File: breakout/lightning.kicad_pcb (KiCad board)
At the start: 2 copper layers, 14 parts, among them J1 CONN_01X02, J2 CONN_01X03, J3 CONN_01X07, U1 AS3935

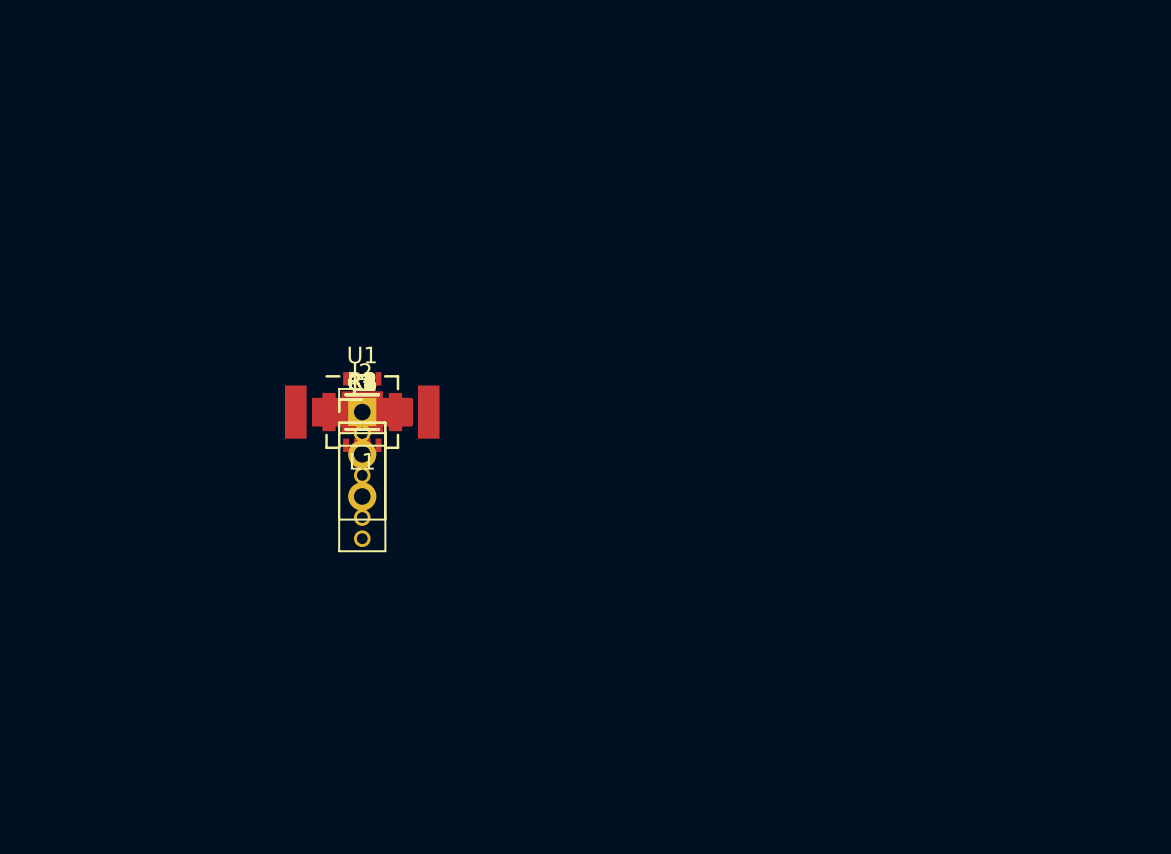
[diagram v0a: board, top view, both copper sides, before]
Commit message: [fix] Wrong size pitch for the connectors.
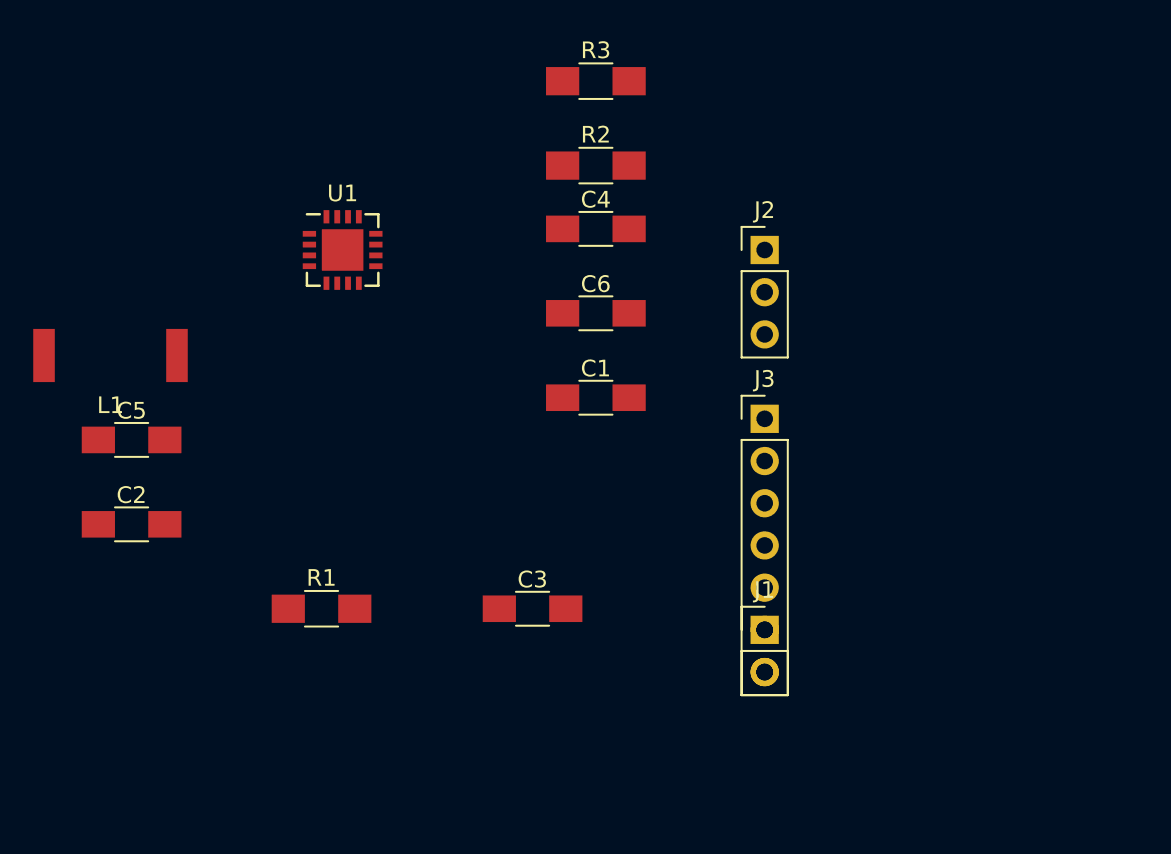
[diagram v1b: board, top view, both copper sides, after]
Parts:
- J1: footprint Pin_Headers:Pin_Header_Straight_1x02_Pitch1.27mm -> Pin_Headers:Pin_Header_Straight_1x02_Pitch2.54mm
- J3: footprint Pin_Headers:Pin_Header_Straight_1x07_Pitch1.27mm -> Pin_Headers:Pin_Header_Straight_1x07_Pitch2.54mm
- moved J1 27.5 mm to (172.7, 118.1)
- moved J2 26.1 mm to (172.7, 95.2)
- moved R3 24.4 mm to (162.6, 85.1)
- moved J3 24.2 mm to (172.7, 105.4)
- moved R2 20.4 mm to (162.6, 90.2)
- moved C4 17.9 mm to (162.6, 94.0)
- moved C3 15.7 mm to (158.8, 116.8)
- moved L1 15.5 mm to (133.3, 101.6)
- moved C2 15.4 mm to (134.6, 111.8)
- moved C6 15.3 mm to (162.6, 99.1)
- moved C1 14.1 mm to (162.6, 104.1)
- moved C5 14.0 mm to (134.6, 106.7)
- moved R1 12.1 mm to (146.1, 116.8)
- moved U1 9.82 mm to (147.3, 95.2)
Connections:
- U1 pad 14: Net-(U1-Pad14) -> (no net)

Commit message: [add] Connections0
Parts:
- J1: value CONN_01X02 -> GS2; footprint Pin_Headers:Pin_Header_Straight_1x02_Pitch2.54mm -> Connectors:GS2
- J2: value CONN_01X03 -> GS3; footprint Pin_Headers:Pin_Header_Straight_1x03_Pitch2.54mm -> Connectors:GS3
- moved C5 51.8 mm to (182.9, 125.5), turned to 270 degrees
- moved L1 46.5 mm to (173.2, 125.5), turned to 180 degrees
- moved U1 41.9 mm to (182.9, 117.3)
- moved C2 40.7 mm to (174.8, 118.4)
- moved R3 39.4 mm to (188.5, 114.8), turned to 270 degrees
- moved C4 36.2 mm to (180.3, 125.5), turned to 270 degrees
- moved C6 34.9 mm to (185.4, 125.5), turned to 90 degrees
- moved R2 30.1 mm to (182.4, 112.8), turned to 180 degrees
- moved J2 29.7 mm to (188.5, 120.4), turned to 180 degrees
- moved R1 28.7 mm to (174.8, 115.8)
- moved J3 21.9 mm to (193.5, 112.3)
- moved C1 20.7 mm to (174.8, 120.9)
- moved J1 17.4 mm to (188.5, 125.5), turned to 180 degrees
- moved C3 16.5 mm to (174.8, 112.8)
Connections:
- J1 pad 1: /CS -> GND
- J1 pad 2: GND -> /CS
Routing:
- net VCC: track 0.00 -> 29.7 mm, vias 0 -> 5
- net Net-(C1-Pad1): track 0.00 -> 24.9 mm
- net /SDA/MOSB: track 0.00 -> 24.2 mm, vias 0 -> 2
- net GND: track 0.00 -> 23.8 mm, vias 0 -> 3
- net /CS: track 0.00 -> 19.2 mm
- net /MISO: track 0.00 -> 14.2 mm, vias 0 -> 2
- net /SCL: track 0.00 -> 12.6 mm, vias 0 -> 2
- net /IRQ: track 0.00 -> 9.59 mm, vias 0 -> 2
- net Net-(C3-Pad2): track 0.00 -> 6.21 mm
- net /SI: track 0.00 -> 5.10 mm
- net Net-(C5-Pad1): track 0.00 -> 4.26 mm
- added copper zone on F.Cu, net GND
- added copper zone on B.Cu, net VCC
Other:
- board outline added: 27.9 x 19.3 mm
- board text added: "CS"
- board text added: "GND"
- board text added: "IRQ"
- board text added: "MISO"
- board text added: "SCL"
- board text added: "SDA"
- board text added: "VCC"

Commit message: [enh] Logos on board
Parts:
- added G***: LOGO, LOGO, B.Cu at (154.9, 95.2)
- added REF***: OSHW-Logo2_9.8x8mm_SilkScreen, Symbols:OSHW-Logo2_9.8x8mm_SilkScreen, B.Cu at (147.3, 95.2)
- moved C1 35.0 mm to (149.6, 96.5)
- moved C2 35.0 mm to (149.6, 94.0)
- moved C3 35.0 mm to (149.6, 88.4)
- moved C4 35.0 mm to (155.2, 101.1)
- moved J3 35.0 mm to (168.4, 87.9)
- moved L1 35.0 mm to (148.1, 101.1)
- moved R1 35.0 mm to (149.6, 91.4)
- moved R2 35.0 mm to (157.2, 88.4)
- moved C5 35.0 mm to (157.7, 101.1)
- moved C6 35.0 mm to (160.3, 101.1)
- moved J1 35.0 mm to (163.3, 101.1)
- moved J2 35.0 mm to (163.3, 96.0)
- moved R3 35.0 mm to (163.3, 90.4)
- moved U1 35.0 mm to (157.7, 93.0)
